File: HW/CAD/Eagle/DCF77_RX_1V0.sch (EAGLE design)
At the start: 37 parts, among them IC251 LMH6645MF, IC271 LMH6645MF, J131 2SK3557, Q211 QT26V-77.000k, X101 PHOENIX_1990067_1X8X2MM50_PTS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, X391 PHOENIX_1990067_1X8X2MM50_PTS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

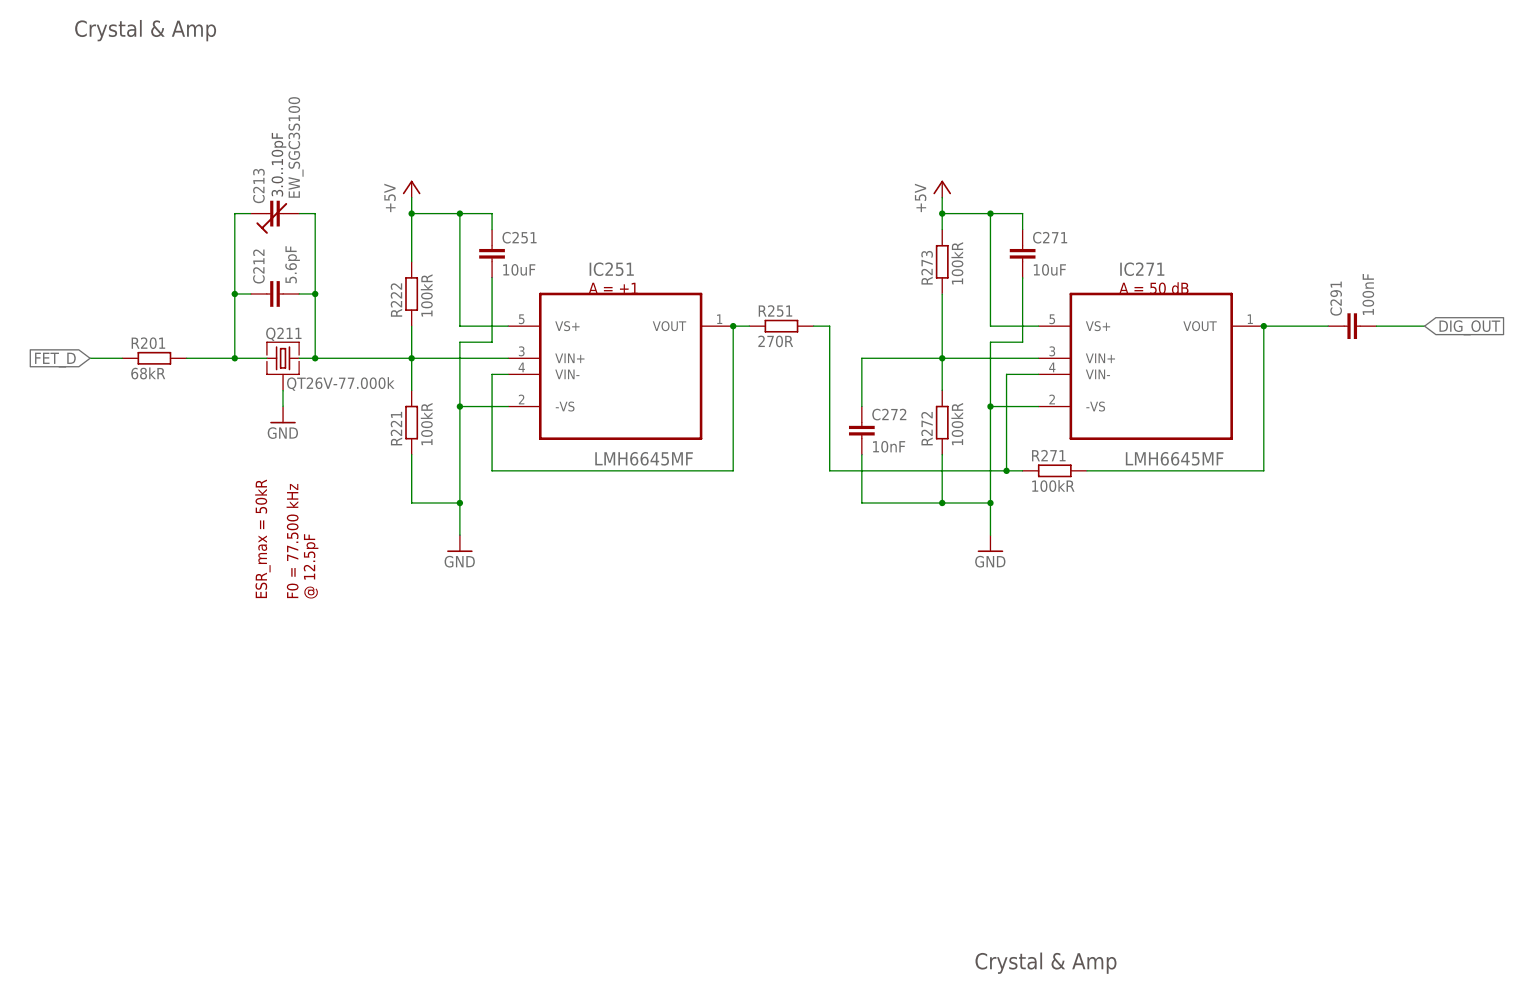
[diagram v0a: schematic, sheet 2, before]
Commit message: HW - Eagle - adaptions from simulation made, layout to do
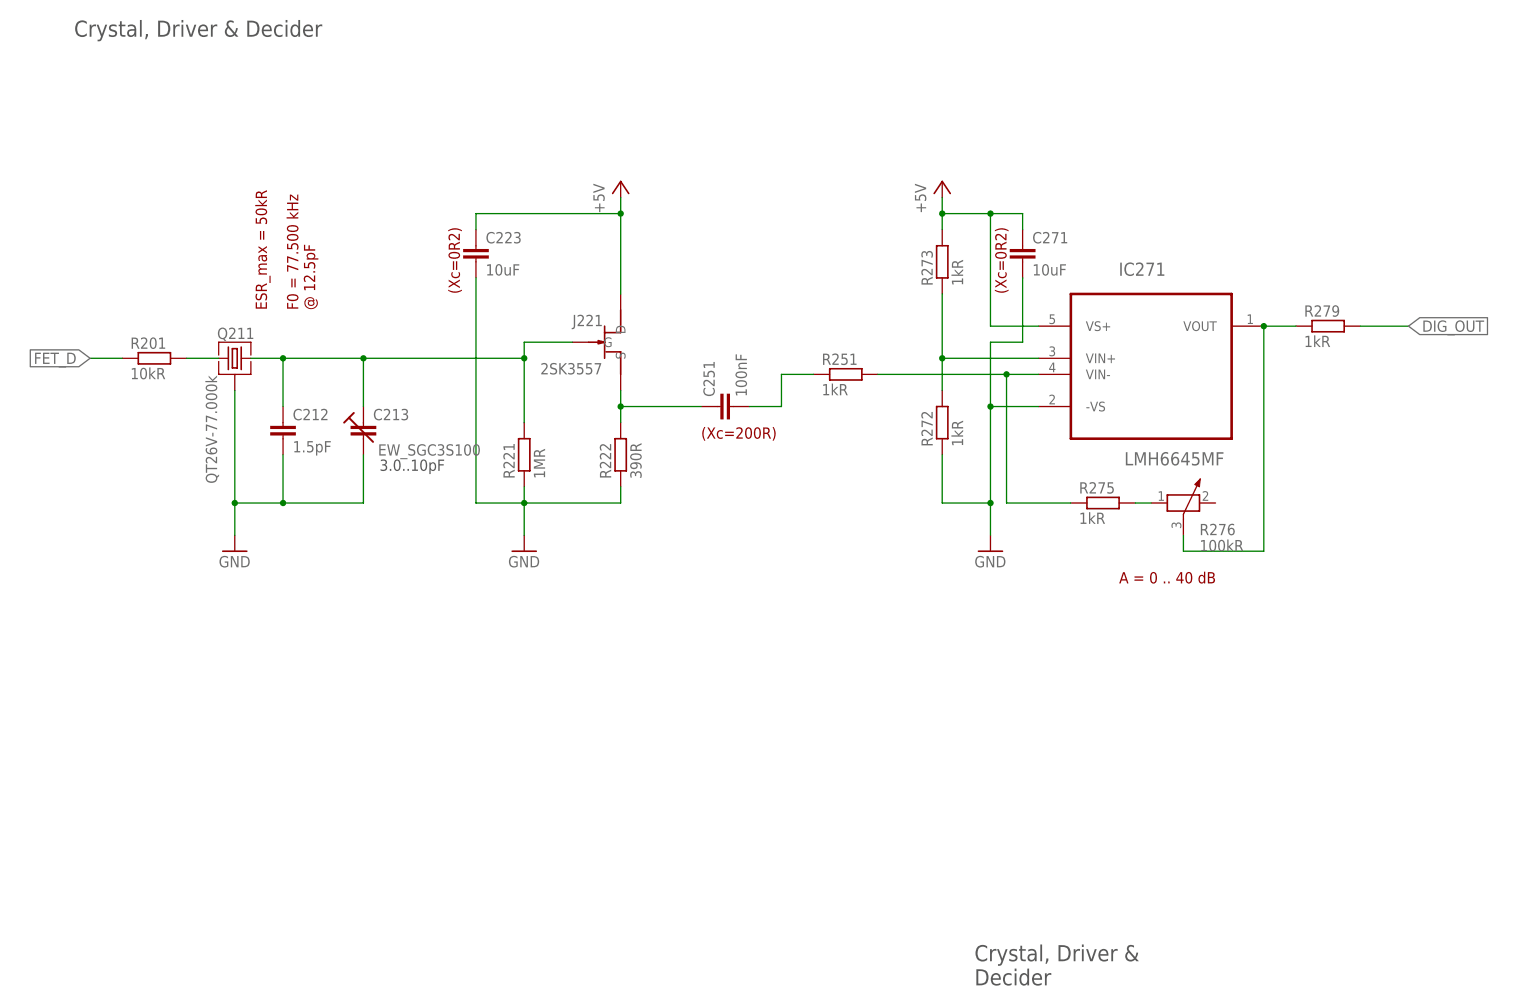
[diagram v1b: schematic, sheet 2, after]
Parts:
- removed C272: 10nF, df4iah_rcl:C-EUC0805
- removed C291: 100nF, df4iah_rcl:C-EUC0805
- removed IC251: LMH6645MF, df4iah_opamp:LMH6645MF
- removed R271: 100kR, df4iah_rcl:R-EU_R0805
- added C223: 10uF, df4iah_rcl:C-EUC0805
- added C395: 47pF, df4iah_rcl:C-EUC0805
- added J221: 2SK3557, df4iah_jfet:2SK3557_N-JFET
- added R275, R279: 1kR, df4iah_rcl:R-EU_R0805
- added R276: 100kR, df4iah_rcl:POTENTIOMETER_PT-10
- C111: value 6.8pF -> 10pF
- C121, C122: value 1nF -> 10nF
- C132: value 1uF -> 2.2uF
- C133: value 4.7uF -> 10uF
- C134: value 100nF -> 2.2nF
- C212: value 5.6pF -> 1.5pF
- C251: value 10uF -> 100nF
- R201: value 68kR -> 10kR
- R221: value 100kR -> 1MR
- R222: value 100kR -> 390R
- R251: value 270R -> 1kR
- R272, R273: value 100kR -> 1kR
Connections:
- removed net N211: C212.1, C213.CROT, Q211.1, R201.2
- new net N$2: Q211.1, R201.2
- new net N222: C251.1, J221.S, R222.2
- new net N275: R275.2, R276.1
- net +5V: now also C223.1, J221.D; no longer C251.1, IC251.VS+, R222.2
- net DIG_OUT: now also C395.1, R279.2, X391.7; no longer C291.2, X391.8
- net GND: now also C212.2, C213.CSTAT, C223.2, C395.2, R222.1, X391.3, X391.6, X391.8; no longer C251.2, C272.2, IC251.-VS
- net N221: now also C212.1, C213.CROT, J221.G; no longer C212.2, C213.CSTAT, IC251.VIN+, R222.1
- net N251: now also C251.2; no longer IC251.VIN-, IC251.VOUT
- net N271: now also R276.3, R279.1; no longer C291.1, R271.2
- net N272: now also IC271.VIN+, R272.2, R273.1; no longer IC271.VIN-, R251.2, R271.1
- net N273: now also IC271.VIN-, R251.2, R275.1; no longer C272.1, IC271.VIN+, R272.2, R273.1
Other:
- note added: "(Xc=0R2)"
- note added: "(Xc=200R)"
- note added: "(Xc=43kR)"
- note added: "A = 0 .. 40 dB"
- note added: "Crystal, Driver & Decider"
- note added: "Input driver"
- note added: "Signal entry & driver"
- note removed: "(Xc=0R5)"
- note removed: "A = +1"
- note removed: "A = 50 dB"
- note removed: "Crystal & Amp"
- note removed: "Impedance change"
- moved on the sheet: C212, C213, C251, C391, C392, L391, Q211, R221, R222, R251, X391

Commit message: HW - Eagle - Hardware ready for the PCB house V1.0
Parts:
- renumbered IC271 to U271
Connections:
- net N$2 renamed N211
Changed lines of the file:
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@@
 <part name="Q211" library="df4iah_crystal" deviceset="QST_QT26V_77.5KHZ" device="" value="QT26V-77.000k"/>
 <part name="GND201" library="df4iah_supply" deviceset="GND" device=""/>
-<part name="IC271" library="df4iah_opamp" deviceset="LMH6645MF" device=""/>
+<part name="U271" library="df4iah_opamp" deviceset="LMH6645MF" device=""/>
 <part name="C213" library="df4iah_c-trimm" deviceset="C-TRIMM__EW_SGC3S" device="" value="EW_SGC3S100"/>
 <part name="C212" library="df4iah_rcl" deviceset="C-EU" device="C0402" value="1.5pF"/>
@@
 </instance>
 <instance part="GND201" gate="1" x="48.26" y="81.28"/>
-<instance part="IC271" gate="A" x="193.04" y="114.3"/>
+<instance part="U271" gate="A" x="193.04" y="114.3"/>
 <instance part="C213" gate="G$1" x="68.58" y="101.6"/>
 <instance part="C212" gate="G$1" x="55.88" y="101.6"/>
@@
 <wire x1="160.02" y1="88.9" x2="167.64" y2="88.9" width="0.1524" layer="91"/>
 <wire x1="167.64" y1="88.9" x2="167.64" y2="104.14" width="0.1524" layer="91"/>
-<pinref part="IC271" gate="A" pin="-VS"/>
+<pinref part="U271" gate="A" pin="-VS"/>
 <wire x1="167.64" y1="104.14" x2="175.26" y2="104.14" width="0.1524" layer="91"/>
 <wire x1="167.64" y1="104.14" x2="167.64" y2="114.3" width="0.1524" layer="91"/>
@@
 <wire x1="167.64" y1="134.62" x2="172.72" y2="134.62" width="0.1524" layer="91"/>
 <junction x="167.64" y="134.62"/>
-<pinref part="IC271" gate="A" pin="VS+"/>
+<pinref part="U271" gate="A" pin="VS+"/>
 <wire x1="175.26" y1="116.84" x2="167.64" y2="116.84" width="0.1524" layer="91"/>
 <wire x1="167.64" y1="116.84" x2="167.64" y2="134.62" width="0.1524" layer="91"/>
@@
 <pinref part="R272" gate="G$1" pin="2"/>
 <wire x1="160.02" y1="106.68" x2="160.02" y2="111.76" width="0.1524" layer="91"/>
-<pinref part="IC271" gate="A" pin="VIN+"/>
+<pinref part="U271" gate="A" pin="VIN+"/>
 <wire x1="160.02" y1="111.76" x2="160.02" y2="121.92" width="0.1524" layer="91"/>
 <wire x1="160.02" y1="111.76" x2="175.26" y2="111.76" width="0.1524" layer="91"/>
@@
 <segment>
 <wire x1="210.82" y1="81.28" x2="210.82" y2="116.84" width="0.1524" layer="91"/>
-<pinref part="IC271" gate="A" pin="VOUT"/>
+<pinref part="U271" gate="A" pin="VOUT"/>
 <wire x1="210.82" y1="81.28" x2="198.12" y2="81.28" width="0.1524" layer="91"/>
 <pinref part="R276" gate="1" pin="3"/>
@@
 </segment>
 </net>
-<net name="N$2" class="0">
+<net name="N211" class="0">
 <segment>
 <pinref part="Q211" gate="G$1" pin="1"/>
@@
 <segment>
 <wire x1="170.18" y1="88.9" x2="170.18" y2="109.22" width="0.1524" layer="91"/>
-<pinref part="IC271" gate="A" pin="VIN-"/>
+<pinref part="U271" gate="A" pin="VIN-"/>
 <wire x1="170.18" y1="109.22" x2="175.26" y2="109.22" width="0.1524" layer="91"/>
 <wire x1="170.18" y1="109.22" x2="149.86" y2="109.22" width="0.1524" layer="91"/>
